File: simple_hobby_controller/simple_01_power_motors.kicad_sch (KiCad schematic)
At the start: 18 parts, among them J1 3S BATTERY XT60, J2 REGULATED 5 V INPUT XT30, J3 LEFT GA25-370 - JST PH 2.0 mm, J4 RIGHT GA25-370 - JST PH 2.0 mm, J5 LEFT MOTOR LARGE SOLDER PADS, J6 RIGHT MOTOR LARGE SOLDER PADS, U1 DRV8848PWP

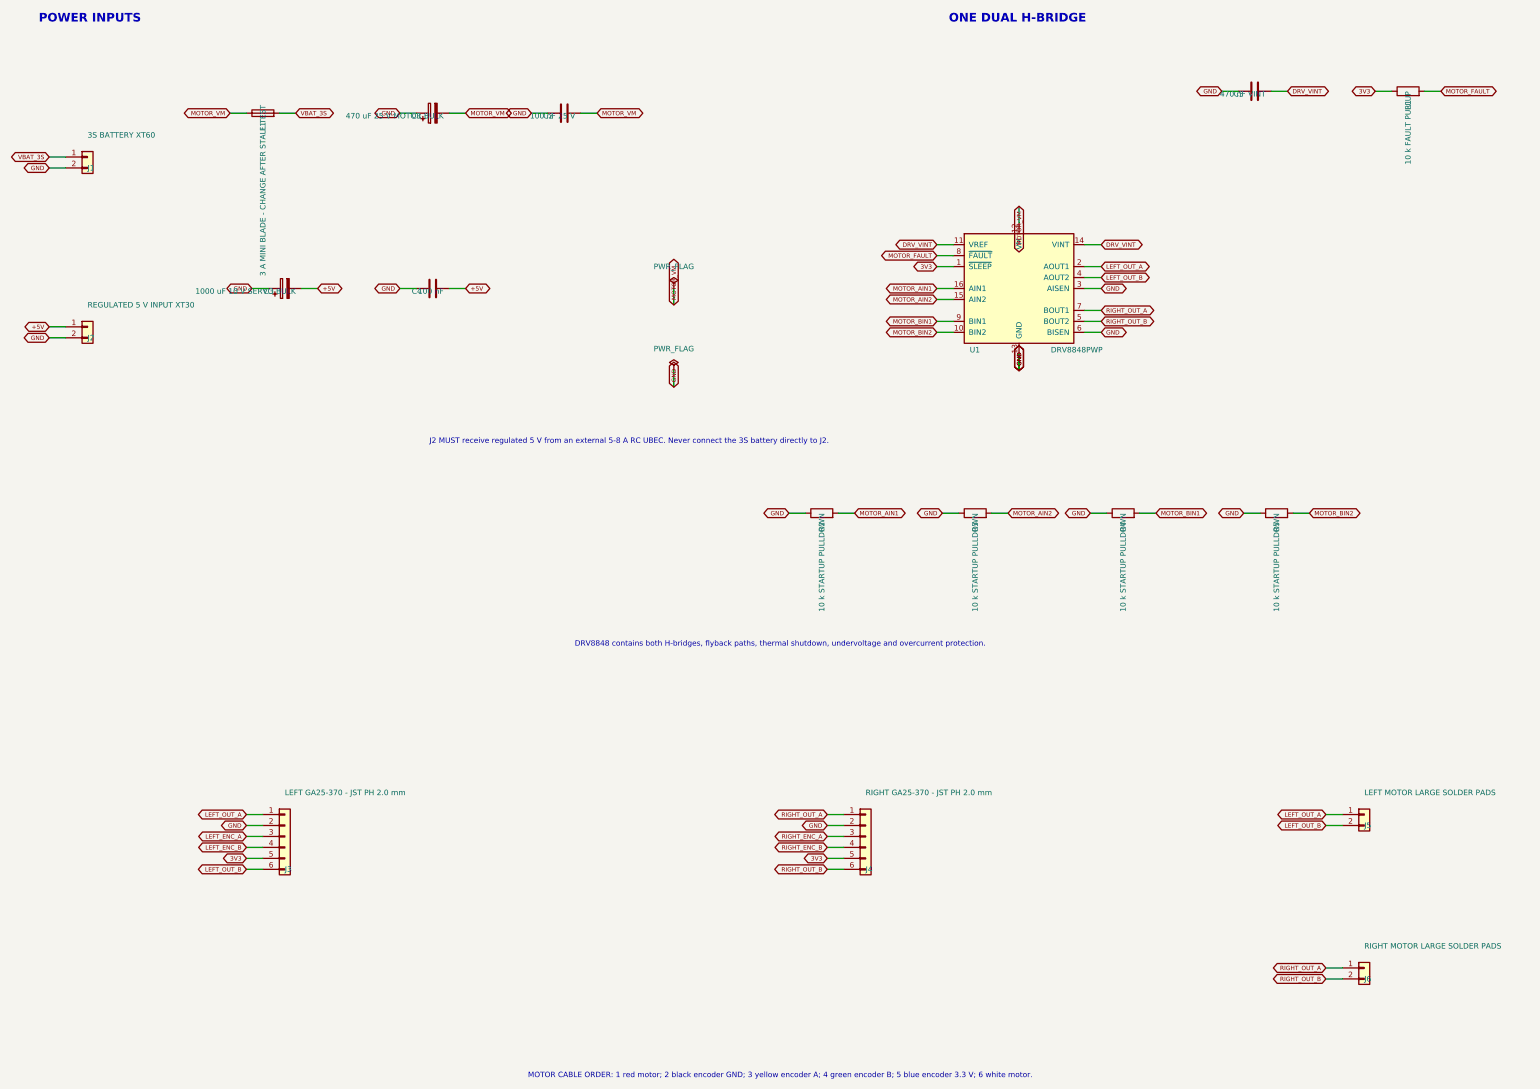
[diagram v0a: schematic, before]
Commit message: Add onboard shared 5V buck rail
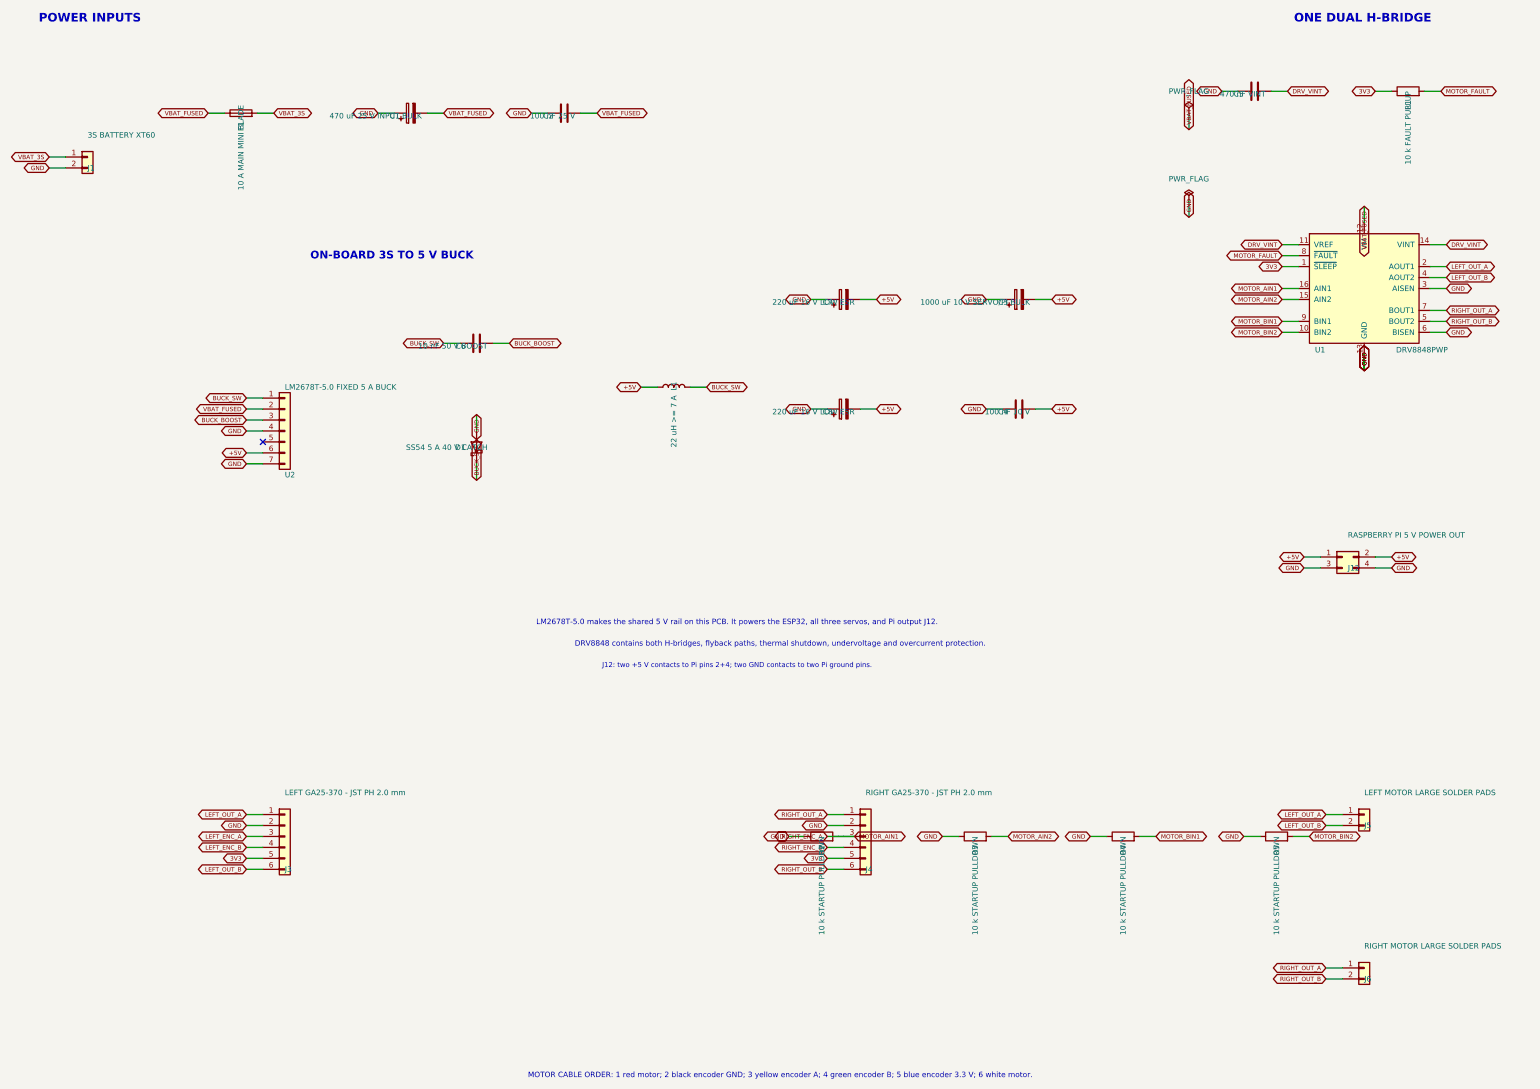
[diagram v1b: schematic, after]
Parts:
- removed J2: REGULATED 5 V INPUT XT30, Connector_AMASS:AMASS_XT30PW-M_1x02_P2.50mm_Horizontal, symbol Connector_Generic:Conn_01x02
- added C6: 10 nF 50 V BOOST, Capacitor_SMD:C_0805_2012Metric, symbol Device:C
- added C7, C8: 220 uF 16 V LOW ESR, Capacitor_THT:CP_Radial_D10.0mm_P5.00mm, symbol Device:C_Polarized
- added D1: SS54 5 A 40 V CATCH, Diode_SMD:D_SMC, symbol Device:D_Schottky
- added J12: RASPBERRY PI 5 V POWER OUT, Connector_Molex:Molex_Micro-Fit_3.0_43045-0415_2x02_P3.00mm_Vertical, symbol Connector_Generic:Conn_02x02_Odd_Even
- added L1: 22 uH >= 7 A, Inductor_SMD:L_Bourns_SRP1770TA_16.9x16.9mm, symbol Device:L
- added U2: LM2678T-5.0 FIXED 5 A BUCK, Package_TO_SOT_THT:TO-220-7_P2.54x5.08mm_StaggerOdd_Lead3.08mm_Vertical, symbol Connector_Generic:Conn_01x07
- C1: value 470 uF 25 V MOTOR BULK -> 470 uF 25 V INPUT BULK
- C3: value 1000 uF 10 V SERVO BULK -> 1000 uF 10 V SERVO/PI BULK
- C4: value 100 nF -> 100 nF 10 V
- F1: value 3 A MINI BLADE - CHANGE AFTER STALL TEST -> 10 A MAIN MINI BLADE
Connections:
- net RIGHT_ENC_A is gone; now on net MOTOR_AIN1: J4.3 (Pin_3)
- net +5V: now also C7.2, C8.2, J12.1 (Pin_1), J12.2 (Pin_2), L1.1, U2.6 (Pin_6)
- net GND: now also C7.1, C8.1, D1.2 (A), J12.3 (Pin_3), J12.4 (Pin_4), U2.4 (Pin_4), U2.7 (Pin_7)
- net MOTOR_VM renamed VBAT_FUSED
- net VBAT_FUSED: now also U2.2 (Pin_2)
- new net BUCK_BOOST: C6.2, U2.3 (Pin_3)
- new net BUCK_SW: C6.1, D1.1 (K), L1.2, U2.1 (Pin_1)
- no-connect marks 0 -> 1
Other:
- note added: "J12: two +5 V contacts to Pi pins 2+4; two GND contacts to two Pi ground pins."
- note added: "LM2678T-5.0 makes the shared 5 V rail on this PCB. It powers the ESP32, all three servos, and Pi output J12."
- note added: "ON-BOARD 3S TO 5 V BUCK"
- note removed: "J2 MUST receive regulated 5 V from an external 5-8 A RC UBEC. Never connect the 3S battery directly to J2."
